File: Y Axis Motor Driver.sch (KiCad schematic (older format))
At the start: 1 part

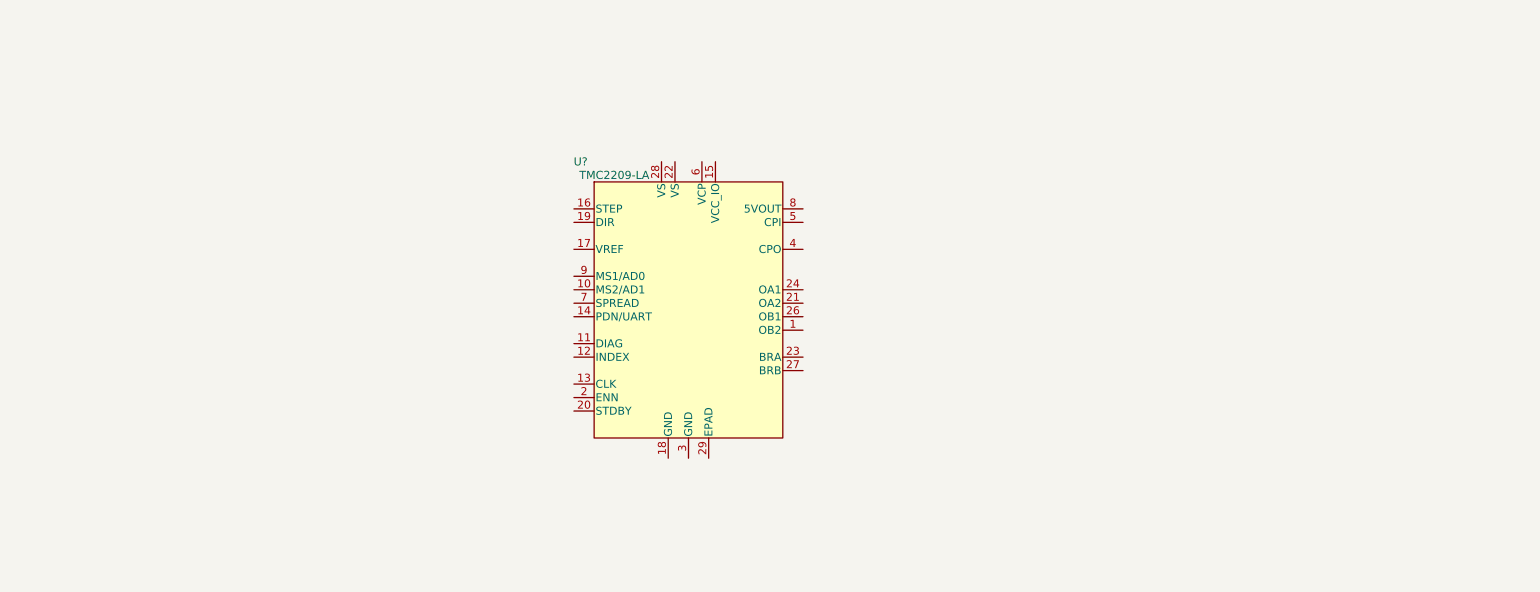
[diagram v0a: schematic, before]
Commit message: Finished TMC2209 schematic for Y and Z motor, added BOM
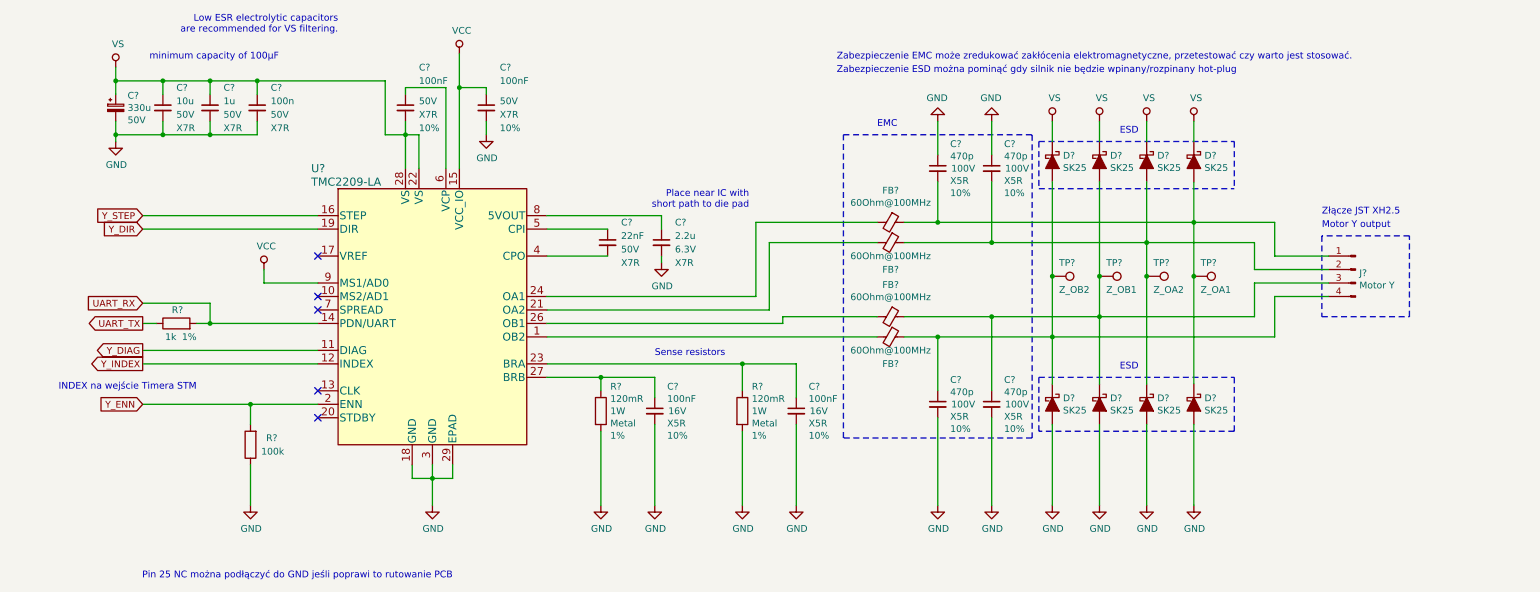
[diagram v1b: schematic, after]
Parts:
- removed U?: TMC2209-LA, footprints:TMC2209-LA, symbol Library:TMC2209-LA
- added C?: 22nF, Capacitor_SMD:C_0603_1608Metric, symbol Device:C_Small
- added C? (x4): 100nF, Capacitor_SMD:C_0603_1608Metric, symbol Device:C_Small
- added C? (x4): 470p, Capacitor_SMD:C_0603_1608Metric, symbol Device:C_Small
- added C?: 330u, symbol Device:CP_Small
- added C?: 10u, symbol Device:C_Small
- added C?: 100n, Capacitor_SMD:C_0603_1608Metric, symbol Device:C_Small
- added C?: 1u, symbol Device:C_Small
- added C?: 2.2u, Capacitor_SMD:C_0603_1608Metric, symbol Device:C_Small
- added D? (x8): SK25, Diode_SMD:D_SMB, symbol Device:D_Schottky_ALT
- added FB? (x4): 60Ohm@100MHz, Inductor_SMD:L_0805_2012Metric, symbol Device:Ferrite_Bead_Small
- added J?: Motor Y, Connector_JST:JST_XH_B4B-XH-AM_1x04_P2.50mm_Vertical, symbol Connector:Conn_01x04_Male
- added R? (x2): 120mR, Resistor_SMD:R_2010_5025Metric, symbol Device:R
- added R?: 1k, Resistor_SMD:R_0603_1608Metric, symbol Device:R
- added R?: 100k, Resistor_SMD:R_0603_1608Metric, symbol Device:R
- added TP?: Z_OB2, symbol Connector:TestPoint
- added TP?: Z_OB1, symbol Connector:TestPoint
- added TP?: Z_OA2, symbol Connector:TestPoint
- added TP?: Z_OA1, symbol Connector:TestPoint
- added U?: TMC2209-LA, footprints:TMC2209-LA, symbol Library:TMC2209-LA
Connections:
- new net: FB?.2, U?.1 (OB2)
- new net: FB?.2, U?.21 (OA2)
- new net: C?.1, R?.1, U?.23 (BRA)
- new net: FB?.2, U?.24 (OA1)
- new net: FB?.2, U?.26 (OB1)
- new net: C?.1, R?.1, U?.27 (BRB)
- new net: C?.2, U?.4 (CPO)
- new net: C?.1, U?.5 (CPI)
- new net: C?.1, U?.6 (VCP)
- new net: C?.1, U?.8 (5VOUT)
- new net: C?.2, D?.1 (K), D?.2 (A), FB?.1, J?.1 (Pin_1), TP?.1
- new net: C?.2, D?.1 (K), D?.2 (A), FB?.1, J?.2 (Pin_2), TP?.1
- new net: C?.1, D?.1 (K), D?.2 (A), FB?.1, J?.3 (Pin_3), TP?.1
- new net: C?.1, D?.1 (K), D?.2 (A), FB?.1, J?.4 (Pin_4), TP?.1
- new net GND: C?.1, C?.1, C?.2, C?.2, C?.2, C?.2, C?.2, C?.2, C?.2, C?.2, C?.2, C?.2, D?.2 (A), D?.2 (A), D?.2 (A), D?.2 (A), R?.1, R?.2, R?.2, U?.18 (GND), U?.29 (EPAD), U?.3 (GND)
- new net UART_RX: R?.2, U?.14 (PDN/UART)
- new net UART_TX: R?.1
- new net VCC: C?.1, U?.15 (VCC_IO), U?.9 (MS1/AD0)
- new net VS: C?.1, C?.1, C?.1, C?.1, C?.2, D?.1 (K), D?.1 (K), D?.1 (K), D?.1 (K), U?.22 (VS), U?.28 (VS)
- new net Y_DIAG: U?.11 (DIAG)
- new net Y_DIR: U?.19 (DIR)
- new net Y_ENN: R?.2, U?.2 (ENN)
- new net Y_INDEX: U?.12 (INDEX)
- new net Y_STEP: U?.16 (STEP)
- no-connect marks 0 -> 5
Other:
- note added: "EMC"
- note added: "ESD"
- note added: "INDEX na wejście Timera STM"
- note added: "Low ESR electrolytic capacitors\nare recommended for VS filtering."
- note added: "Motor Y output"
- note added: "Pin 25 NC można podłączyć do GND jeśli poprawi to rutowanie PCB"
- note added: "Place near IC with\nshort path to die pad"
- note added: "Sense resistors"
- note added: "Zabezpieczenie EMC może zredukować zakłócenia elektromagnetyczne, przetestować czy warto jest stosować."
- note added: "Zabezpieczenie ESD można pominąć gdy silnik nie będzie wpinany/rozpinany hot-plug"
- note added: "Złącze JST XH2.5"
- note added: "minimum capacity of 100μF"
